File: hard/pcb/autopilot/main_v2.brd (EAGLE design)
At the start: 102 x 67 mm, 167 parts, among them IC1 24AA32ASN, IC2 INA194, IC3 LP2950Z, Q1 IRLML5203, Q3 IRLML5203, Q4 IRLML5203, T3 BC848, U2 TMP75DGK, U44 BMP085, X1 USB-SMD-NS

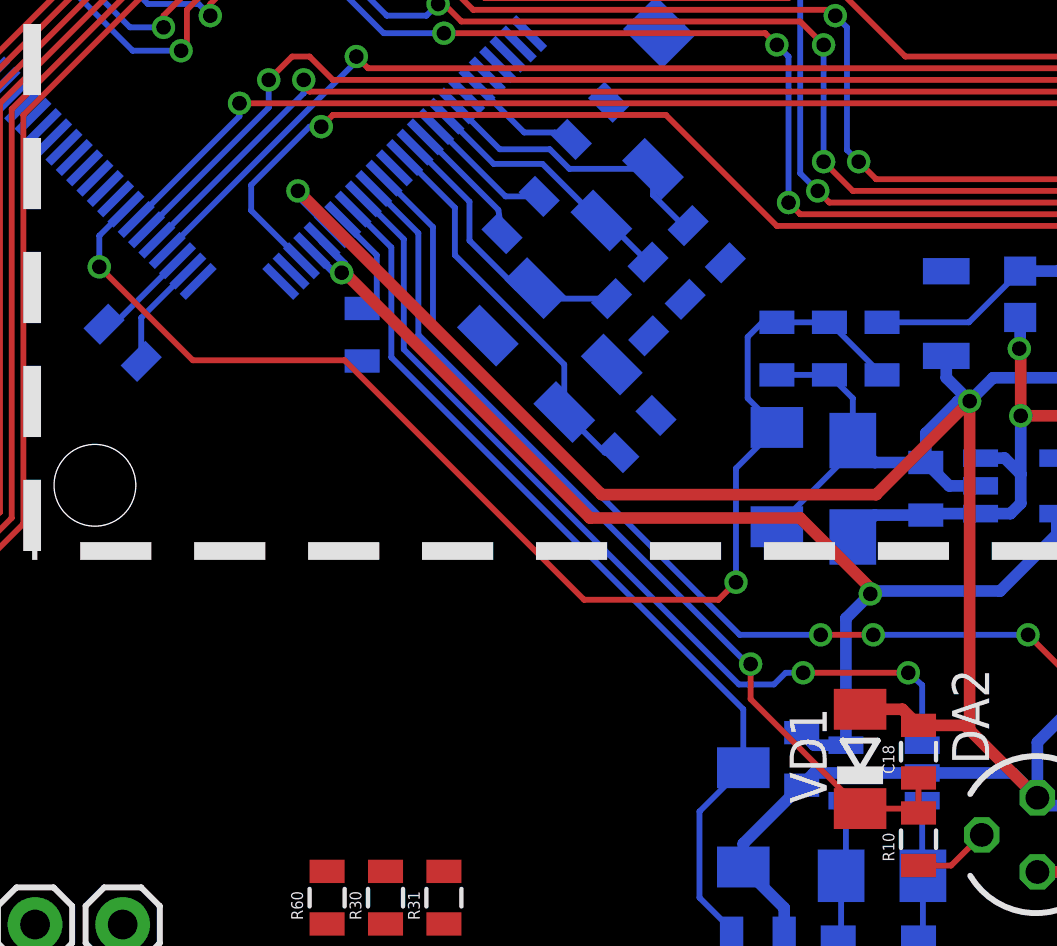
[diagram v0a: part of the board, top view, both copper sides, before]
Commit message: board v2. Added capacitor for ADC
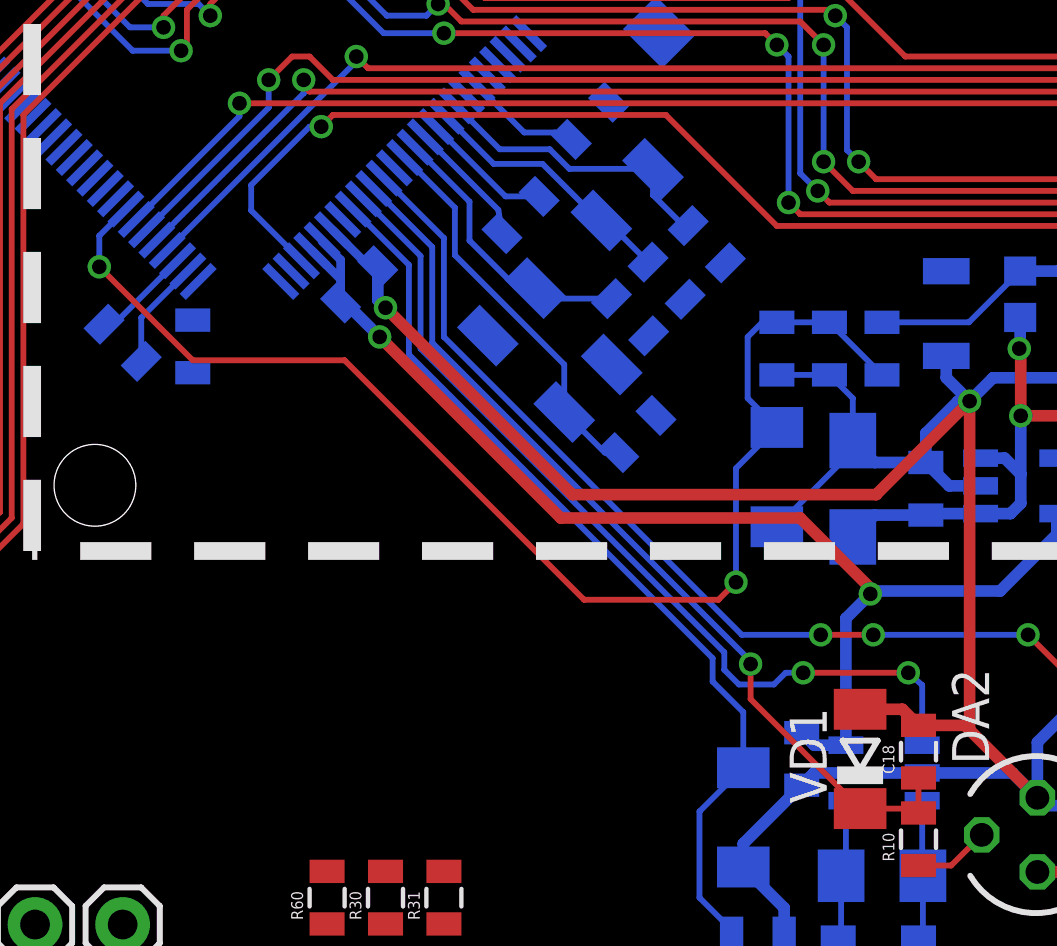
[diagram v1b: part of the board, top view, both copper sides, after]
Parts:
- added C46: 0.1uF, SparkFun:0805
- moved C3 5.81 mm to (51.4, 27.9)
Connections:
- net +3.3V_A: now also C46.1
- net GND_A: now also C46.2
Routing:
- net 3.3V: track 70.2 -> 66.3 mm
- net GND_A: track 139.7 -> 136.9 mm
- net +3.3V_A: track 65.3 -> 65.9 mm

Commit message: nop
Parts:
- moved C6 29.0 mm to (37.6, 34.8), turned to 90 degrees
- moved C3 6.90 mm to (58.0, 25.9)
- moved C44 4.82 mm to (41.4, 36.2), turned to 135 degrees
- moved C46 0.50 mm to (56.7, 29.7)
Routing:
- net 3.3V: track 66.3 -> 70.3 mm
- net N$82: track 3.64 -> 2.00 mm
- net +3.3V_A: track 65.9 -> 65.4 mm

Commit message: Board v2. Nop
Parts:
- moved C6 30.2 mm to (66.2, 44.6), turned to 225 degrees
- moved R15 11.7 mm to (38.8, 10.6), turned to 90 degrees
- moved C13 9.99 mm to (3.60, 48.4), turned to 180 degrees
- moved Q3 8.05 mm to (35.8, 10.6), turned to 270 degrees
- moved R32 7.41 mm to (69.4, 34.6), turned to 225 degrees
- moved R1 6.96 mm to (31.4, 20.8), flipped to the top, turned to 90 degrees
- moved C7 5.80 mm to (33.2, 7.40), turned to 180 degrees
- moved C8 5.31 mm to (32.6, 10.6), turned to 180 degrees
- moved F1 1.81 mm to (22.6, 55.2)
- moved C4 1.28 mm to (50.0, 28.8)
- moved C2 1.08 mm to (41.6, 40.2)
- moved C38 1.08 mm to (64.6, 43.0)
- moved R7 1.00 mm to (11.4, 45.2)
- moved C44 0.72 mm to (41.0, 36.8)
- moved C40 0.60 mm to (65.0, 36.2)
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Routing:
- net 3.3V: track 70.3 -> 219.8 mm, vias 1 -> 8
- net RESET: track 0.00 -> 62.2 mm, vias 0 -> 3
- net SDC_PWR_EN: track 0.00 -> 57.0 mm, vias 0 -> 2
- net TIM1_CH1: track 0.00 -> 47.8 mm, vias 0 -> 1
- net TIM1_CH2: track 0.00 -> 44.0 mm, vias 0 -> 1
- net TIM1_CH3: track 0.00 -> 39.2 mm, vias 0 -> 1
- net TIM1_CH4: track 0.00 -> 35.0 mm, vias 0 -> 1
- net I2C_SLOW_SCL: track 0.00 -> 32.8 mm
- net I2C_SLOW_SDA: track 0.00 -> 32.3 mm
- net SDIO_DETECT: track 0.00 -> 29.7 mm, vias 0 -> 1
- net N$34: track 0.00 -> 9.40 mm
- net N$23: track 0.00 -> 6.81 mm, vias 0 -> 1
- net GND: track 71.3 -> 74.3 mm, vias 2 -> 3
- net GPS_ENABLE: track 53.4 -> 55.2 mm
- net SDIO_D1: track 47.9 -> 49.2 mm
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
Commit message: nop
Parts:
- moved R14 42.9 mm to (80.2, 40.4), flipped to the bottom, turned to 270 degrees
- moved C28 38.8 mm to (74.2, 42.6), flipped to the bottom, turned to 90 degrees
- moved C19 38.3 mm to (81.8, 42.8), flipped to the bottom, turned to 90 degrees
- moved C29 38.2 mm to (77.5, 40.6), flipped to the bottom
- moved DD3 36.1 mm to (77.8, 44.3), flipped to the bottom, turned to 270 degrees
- moved C25 33.0 mm to (81.8, 45.8), flipped to the bottom, turned to 270 degrees
- moved C26 29.5 mm to (77.0, 47.9), flipped to the bottom, turned to 180 degrees
- moved R28 26.5 mm to (65.4, 51.4), turned to 90 degrees
- moved R27 26.4 mm to (67.2, 51.4), turned to 90 degrees
- moved R7 1.97 mm to (10.6, 47.0)
- moved R22 1.17 mm to (7.00, 18.4)
- moved R23 1.02 mm to (7.00, 20.8)
- moved R17 0.57 mm to (6.60, 38.6)
- moved R19 0.57 mm to (6.60, 33.6)
- moved R24 0.57 mm to (6.60, 28.4)
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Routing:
- net TDO: track 0.00 -> 79.0 mm, vias 0 -> 2
- net TRST: track 0.00 -> 73.1 mm, vias 0 -> 2
- net TMS: track 0.00 -> 69.3 mm, vias 0 -> 2
- net TCK: track 0.00 -> 66.2 mm, vias 0 -> 2
- net TDI: track 0.00 -> 65.7 mm, vias 0 -> 2
- net 3.3V: track 219.8 -> 233.1 mm, vias 8 -> 14
- net XBEE_RTS: track 18.6 -> 7.86 mm
- net TIM1_CH3: track 39.2 -> 45.6 mm
- net TIM1_CH2: track 44.0 -> 50.5 mm
- net TIM1_CH1: track 47.8 -> 54.2 mm
- net TIM1_CH4: track 35.0 -> 41.1 mm
- net N$18: track 0.00 -> 3.34 mm
- net N$17: track 0.00 -> 3.30 mm
- net N$19: track 0.00 -> 2.96 mm
- net RESET: track 62.2 -> 60.1 mm, vias 3 -> 5
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
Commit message: nop
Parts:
- moved C27 73.5 mm to (86.0, 36.0), turned to 90 degrees
- moved R25 71.8 mm to (68.2, 51.6), turned to 90 degrees
- moved U44 71.6 mm to (81.7, 37.1), turned to 90 degrees
- moved R11 69.2 mm to (66.6, 51.6), turned to 90 degrees
- moved Q4 68.5 mm to (77.0, 49.0), turned to 90 degrees
- moved C35 68.0 mm to (29.0, 41.0)
- moved C30 67.8 mm to (26.2, 39.0)
- moved C21 67.7 mm to (80.2, 48.2)
- moved U2 67.7 mm to (67.8, 46.7), turned to 180 degrees
- moved DD5 67.7 mm to (28.9, 37.4)
- moved IC1 67.6 mm to (77.9, 44.5)
- moved C36 67.5 mm to (32.0, 38.8)
- moved C32 67.0 mm to (32.0, 35.8), turned to 90 degrees
- moved R75 65.1 mm to (80.8, 33.2), turned to 180 degrees
- moved R16 65.0 mm to (74.4, 49.0), turned to 270 degrees
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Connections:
- net I2C_FAST_SCL: now also DD1.47; no longer DD1.92
- net I2C_FAST_SDA: now also DD1.48; no longer DD1.93
- net I2C_SLOW_SCL: now also DD1.92; no longer DD1.47
- net I2C_SLOW_SDA: now also DD1.93; no longer DD1.48
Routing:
- net 3.3V: track 233.1 -> 275.3 mm, vias 14 -> 16
- net RESET: track 60.1 -> 97.6 mm, vias 5 -> 7
- net BMP085_EOC: track 0.00 -> 23.9 mm
- net GND: track 74.3 -> 92.8 mm
- net N$25: track 0.00 -> 5.95 mm
- net I2C_FAST_SDA: track 0.00 -> 4.59 mm
- net I2C_FAST_SCL: track 0.00 -> 3.05 mm
- net N$28: track 0.00 -> 2.14 mm
- net N$22: track 0.00 -> 2.14 mm
- net N$27: track 0.00 -> 1.87 mm
- net N$24: track 0.00 -> 1.84 mm
- net N$74: track 0.00 -> 1.83 mm
- net N$26: track 0.00 -> 1.69 mm
- net EEPROM_PWR_EN: track 0.00 -> 1.68 mm
- net N$21: track 0.00 -> 1.60 mm
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
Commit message: nop
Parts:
- removed R26, R37: 0, SparkFun:0805
- added U$2: (no value), barthess:LOGO_CHIBIOS_SILK
- added VD5: BAR43, barthess:SOT23-3
- moved C19 57.3 mm to (13.0, 74.0), turned to 270 degrees
- moved R14 56.4 mm to (14.6, 76.2), turned to 90 degrees
- moved C25 55.9 mm to (13.0, 71.0), turned to 90 degrees
- moved C29 53.0 mm to (17.3, 76.2), turned to 0 degrees
- moved DD3 51.3 mm to (17.0, 72.5), turned to 90 degrees
- moved C26 48.6 mm to (17.8, 68.9), turned to 0 degrees
- moved C28 47.6 mm to (20.6, 74.2), turned to 270 degrees
- moved JP4 46.3 mm to (26.4, 74.6)
- moved JP5 46.3 mm to (26.4, 71.6)
- moved LED1 46.3 mm to (26.4, 77.1)
- moved LED2 46.3 mm to (26.4, 69.1)
- moved R2 46.3 mm to (32.4, 69.1)
- moved R3 46.3 mm to (32.4, 77.1)
- moved R4 46.3 mm to (29.4, 69.1)
- moved R5 46.3 mm to (29.4, 77.1)
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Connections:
- removed net N$31: DD1.53, R26.2, R37.2
- removed net XBEE_RTS: JP1.6, R37.1
- net 3.3V: now also VD5.1
- net N$33: now also VD5.3
- net SPI2_MISO_UEXT: now also DD1.53; no longer R26.1
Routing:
- net SPI2_NSS_UEXT: track 0.00 -> 50.2 mm
- net SPI2_MOSI_UEXT: track 0.00 -> 47.6 mm
- net USART6_RX_UEXT: track 0.00 -> 46.5 mm
- net SPI2_SCK_UEXT: track 0.00 -> 46.1 mm
- net USART6_TX_UEXT: track 0.00 -> 44.6 mm
- net SPI2_MISO_UEXT: track 0.00 -> 44.5 mm
- net I2C_SLOW_SDA: track 32.9 -> 42.8 mm
- net XBEE_RTS: track 7.86 -> 0.00 mm, vias 1 -> 0
- net I2C_SLOW_SCL: track 34.3 -> 40.4 mm
- net RESET: track 97.6 -> 100.6 mm
- net N$54: track 43.1 -> 40.6 mm

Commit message: nop
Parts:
- moved C6 19.0 mm to (53.2, 26.4), turned to 90 degrees
- moved VD4 3.88 mm to (12.6, 13.2)
- moved VD5 3.41 mm to (12.6, 16.8), turned to 90 degrees
- moved C20 2.28 mm to (64.6, 48.4)
- moved U2 1.89 mm to (67.2, 47.9)
- moved C38 1.02 mm to (65.2, 42.8), turned to 90 degrees
- moved U$2 0.72 mm to (60.4, 10.4)
- moved C4 0.63 mm to (49.4, 29.0)
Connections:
- removed net TMP75_ALERT: DD1.5, U2.3
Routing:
- net N$33: track 3.75 -> 62.3 mm, vias 0 -> 2
- net AD_CLK: track 0.00 -> 57.5 mm, vias 0 -> 1
- net MPU9150_INT: track 0.00 -> 34.7 mm, vias 0 -> 3
- net MAG_INT: track 0.00 -> 30.6 mm
- net FROM_GPS: track 59.8 -> 41.5 mm, vias 4 -> 3
- net TO_GPS: track 59.4 -> 41.5 mm, vias 3 -> 2
- net I2C_FAST_SCL: track 3.05 -> 18.5 mm, vias 0 -> 1
- net 3.3V: track 275.7 -> 263.1 mm, vias 16 -> 14
- net I2C_FAST_SDA: track 4.59 -> 16.5 mm, vias 0 -> 1
- net I2C_SLOW_SDA: track 42.8 -> 31.3 mm
- net I2C_SLOW_SCL: track 40.4 -> 29.3 mm
- net RECEIVER_PPM: track 51.9 -> 49.8 mm
- net ADIS_INT: track 34.8 -> 36.7 mm
- net GND: track 92.8 -> 94.1 mm

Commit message: nop
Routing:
- net EEPROM_PWR_EN: track 1.68 -> 35.7 mm, vias 0 -> 2
- net TO_GPS: track 41.5 -> 63.1 mm, vias 2 -> 3
- net FROM_GPS: track 41.5 -> 62.6 mm, vias 3 -> 4
- net SDIO_D2: track 54.0 -> 41.5 mm
- net I2C_SLOW_SDA: track 31.3 -> 43.7 mm
- net I2C_SLOW_SCL: track 29.3 -> 40.7 mm
- net TDO: track 79.0 -> 80.2 mm
- net GPS_ENABLE: track 53.4 -> 52.6 mm
- net RESET: track 100.6 -> 101.2 mm
